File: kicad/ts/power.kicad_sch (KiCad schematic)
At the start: 28 parts, among them J1 JPWR

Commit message: update footprints
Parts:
- F0, F1, F2, G0, G1, G10, G2, G3, G4, G6, G7, G8, G9, TS1: footprint (none) -> Package_DIP:DIP-14_W7.62mm
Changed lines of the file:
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@@
 			)
 		)
-		(property "Footprint" ""
+		(property "Footprint" "Package_DIP:DIP-14_W7.62mm"
 			(at 90.805 163.83 0)
 			(effects
@@
 			)
 		)
-		(property "Footprint" ""
+		(property "Footprint" "Package_DIP:DIP-14_W7.62mm"
 			(at 79.375 163.83 0)
 			(effects
@@
 			)
 		)
-		(property "Footprint" ""
+		(property "Footprint" "Package_DIP:DIP-14_W7.62mm"
 			(at 56.515 124.46 0)
 			(effects
@@
 			)
 		)
-		(property "Footprint" ""
+		(property "Footprint" "Package_DIP:DIP-14_W7.62mm"
 			(at 56.515 205.105 0)
 			(effects
@@
 			)
 		)
-		(property "Footprint" ""
+		(property "Footprint" "Package_DIP:DIP-14_W7.62mm"
 			(at 45.085 205.105 0)
 			(effects
@@
 			)
 		)
-		(property "Footprint" ""
+		(property "Footprint" "Package_DIP:DIP-14_W7.62mm"
 			(at 33.655 124.46 0)
 			(effects
@@
 			)
 		)
-		(property "Footprint" ""
+		(property "Footprint" "Package_DIP:DIP-14_W7.62mm"
 			(at 90.805 205.105 0)
 			(effects
@@
 			)
 		)
-		(property "Footprint" ""
+		(property "Footprint" "Package_DIP:DIP-14_W7.62mm"
 			(at 45.085 163.83 0)
 			(effects
@@
 			)
 		)
-		(property "Footprint" ""
+		(property "Footprint" "Package_DIP:DIP-14_W7.62mm"
 			(at 45.085 124.46 0)
 			(effects
@@
 			)
 		)
-		(property "Footprint" ""
+		(property "Footprint" "Package_DIP:DIP-14_W7.62mm"
 			(at 79.375 205.105 0)
 			(effects
@@
 			)
 		)
-		(property "Footprint" ""
+		(property "Footprint" "Package_DIP:DIP-14_W7.62mm"
 			(at 33.655 163.83 0)
 			(effects
@@
 			)
 		)
-		(property "Footprint" ""
+		(property "Footprint" "Package_DIP:DIP-14_W7.62mm"
 			(at 56.515 163.83 0)
 			(effects
@@
 			)
 		)
-		(property "Footprint" ""
+		(property "Footprint" "Package_DIP:DIP-14_W7.62mm"
 			(at 67.945 163.83 0)
 			(effects
@@
 			)
 		)
-		(property "Footprint" ""
+		(property "Footprint" "Package_DIP:DIP-14_W7.62mm"
 			(at 67.945 205.105 0)
 			(effects

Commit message: Schemativ corrections, work started on pcb
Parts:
- G5: footprint (none) -> Package_DIP:DIP-14_W7.62mm
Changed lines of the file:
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@@
 			)
 		)
-		(property "Footprint" ""
+		(property "Footprint" "Package_DIP:DIP-14_W7.62mm"
 			(at 33.655 205.105 0)
 			(effects

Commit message: Schematic corrections, all pcb traces placed, todo footprints check
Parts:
- CPWR1: footprint Capacitor_THT:CP_Radial_D10.0mm_P3.50mm -> Capacitor_THT:CP_Radial_D7.5mm_P2.50mm
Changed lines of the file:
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@@
 			)
 		)
-		(property "Footprint" "Capacitor_THT:CP_Radial_D10.0mm_P3.50mm"
+		(property "Footprint" "Capacitor_THT:CP_Radial_D7.5mm_P2.50mm"
 			(at 51.435 57.15 0)
 			(effects

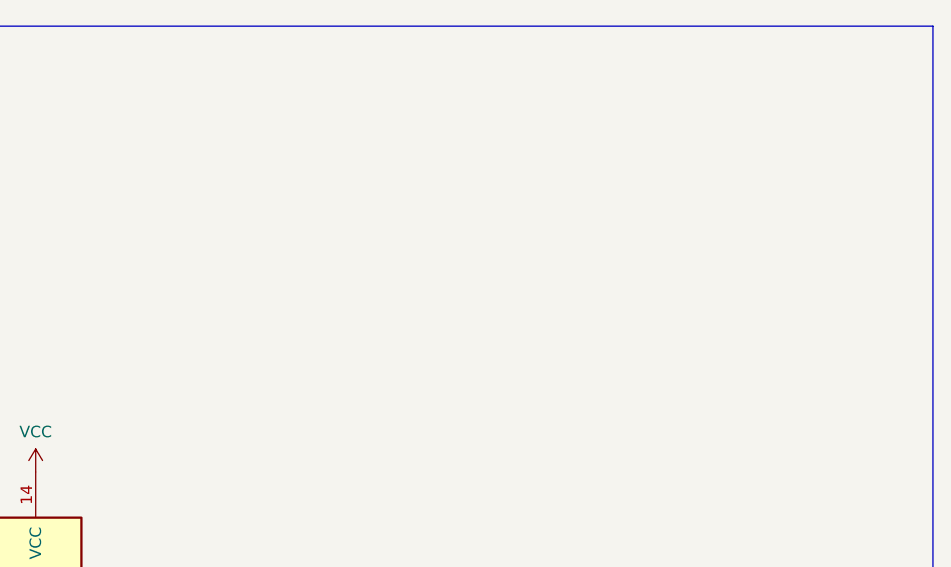
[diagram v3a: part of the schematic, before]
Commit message: Add mounting holes, update README, new image
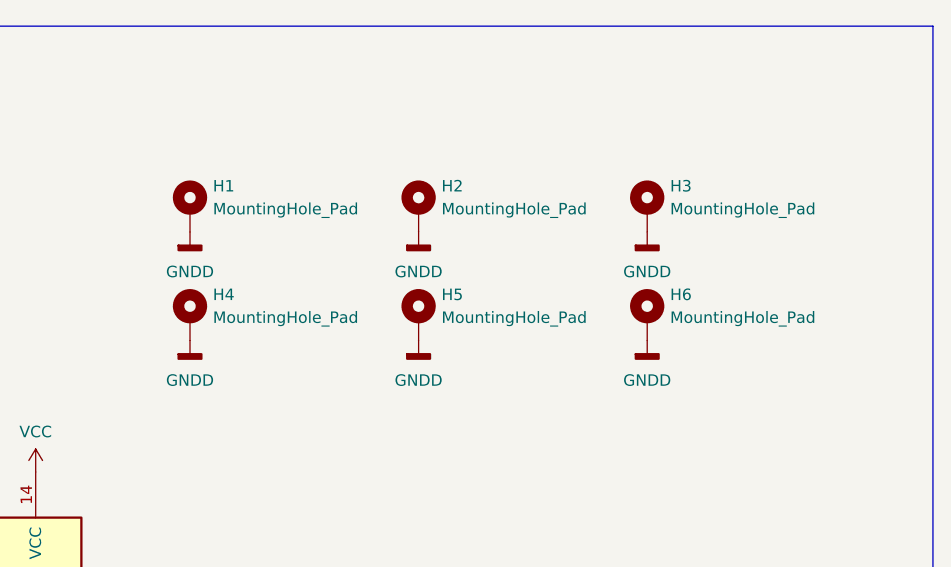
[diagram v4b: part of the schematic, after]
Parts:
- added H1, H2, H3, H4, H5, H6: MountingHole_Pad, MountingHole:MountingHole_3.2mm_M3_DIN965_Pad, symbol Mechanical:MountingHole_Pad
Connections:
- net GNDD: now also H1.1, H2.1, H3.1, H4.1, H5.1, H6.1
